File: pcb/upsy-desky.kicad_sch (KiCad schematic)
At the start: 44 parts, among them J1 RJ45, J2 RJ45, J3 USB_C_ReceptacleUSB2.0, Q1 MMBT3904, Q2 MMBT3904, Q3 2N7002, Q4 2N7002, Q5 2N7002, Q6 2N7002, Q7 2N7002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

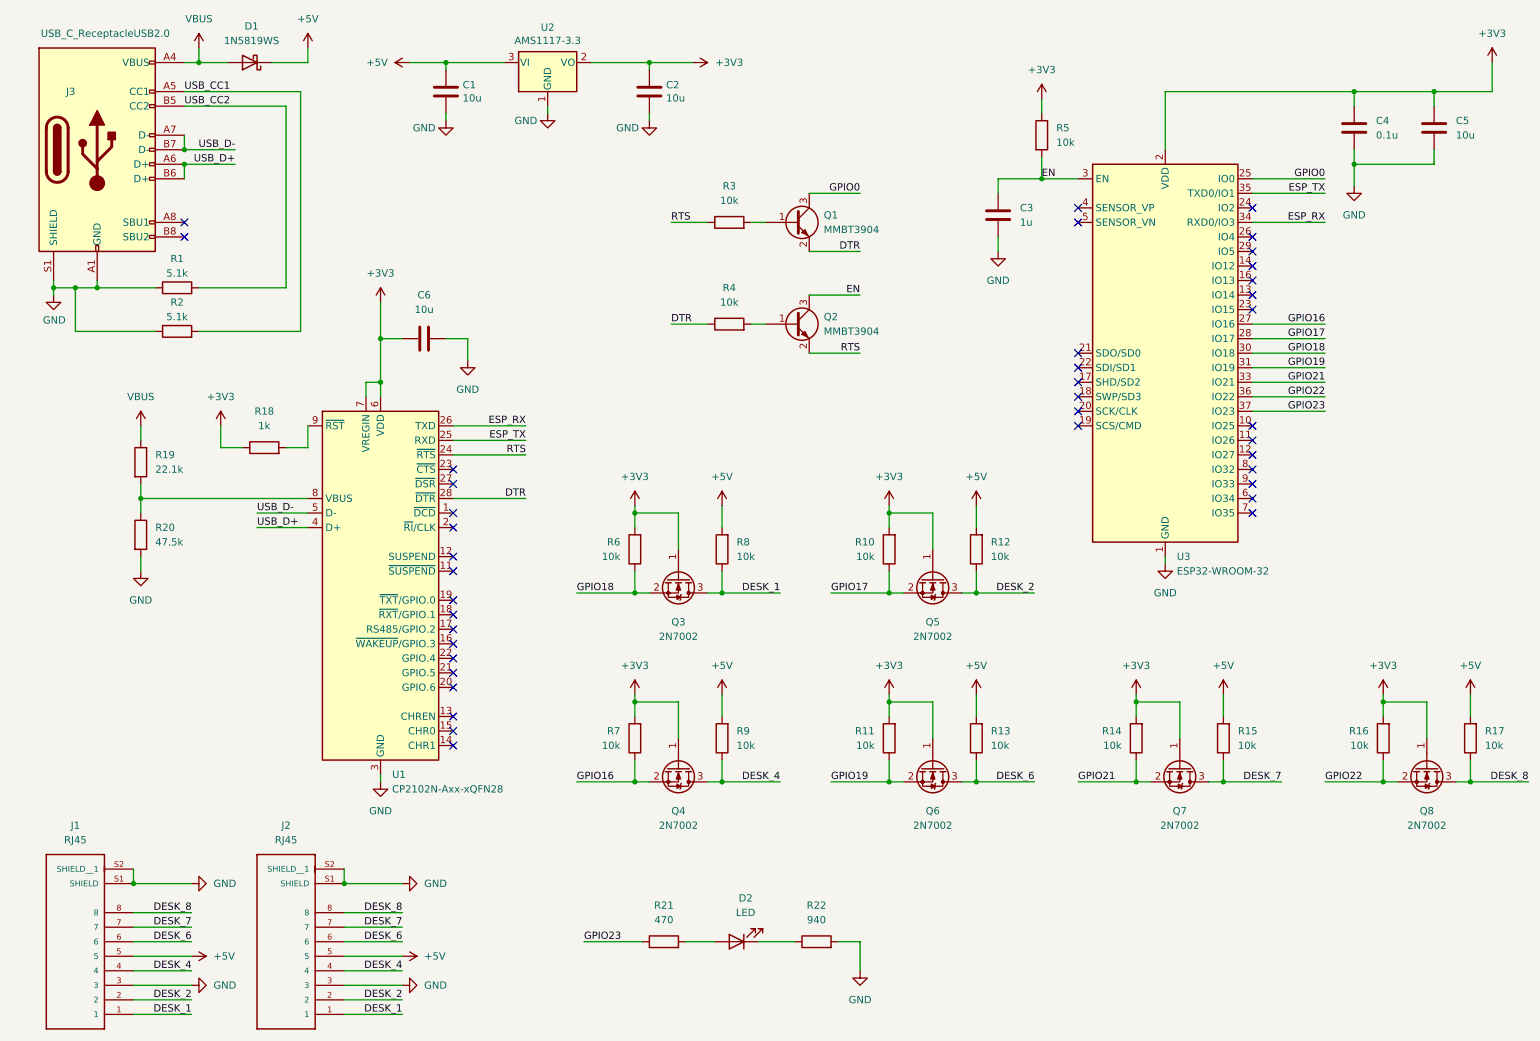
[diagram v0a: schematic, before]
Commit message: Adding updated PCB files using ESP32-s3-WROOM-1 MCU, removed UART to USB logic
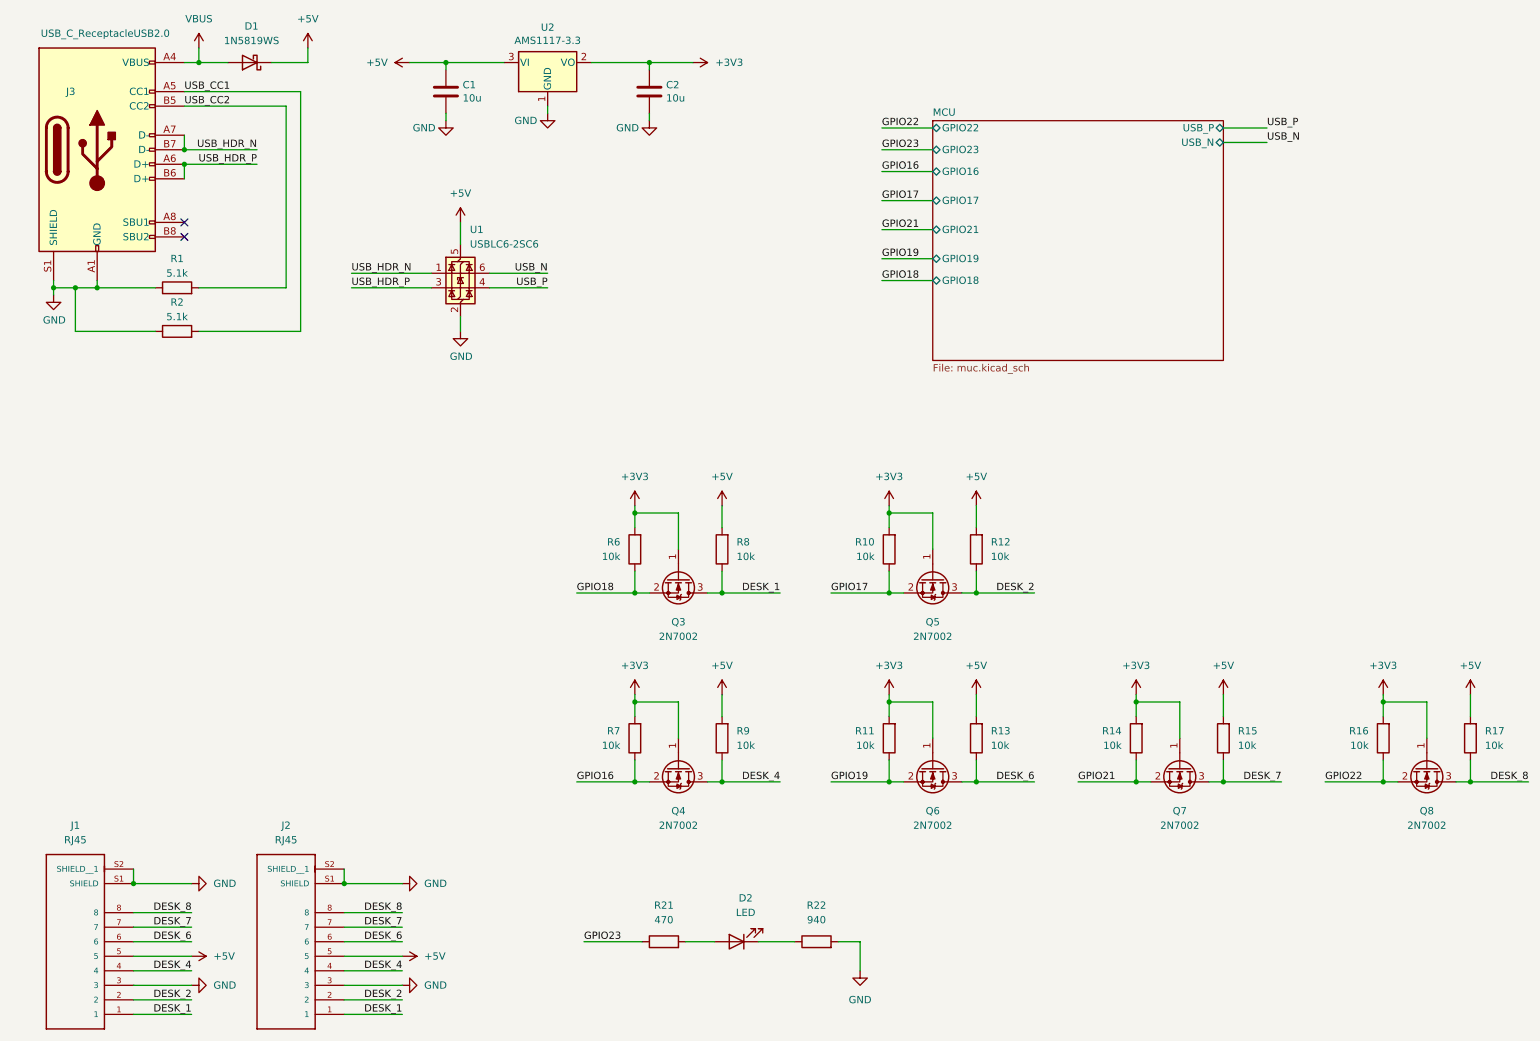
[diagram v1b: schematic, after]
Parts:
- removed C3: 1u, Capacitor_SMD:C_0402_1005Metric, symbol Device:C
- removed C4: 0.1u, Capacitor_SMD:C_0402_1005Metric, symbol Device:C
- removed C5, C6: 10u, Capacitor_SMD:C_0402_1005Metric, symbol Device:C
- removed Q1, Q2: MMBT3904, Package_TO_SOT_SMD:SOT-23, symbol Transistor_BJT:MMBT3904
- removed R18: 1k, Resistor_SMD:R_0402_1005Metric, symbol Device:R
- removed R19: 22.1k, Resistor_SMD:R_0402_1005Metric, symbol Device:R
- removed R20: 47.5k, Resistor_SMD:R_0402_1005Metric, symbol Device:R
- removed R3, R4, R5: 10k, Resistor_SMD:R_0402_1005Metric, symbol Device:R
- removed U1: CP2102N-Axx-xQFN28, Package_DFN_QFN:QFN-28-1EP_5x5mm_P0.5mm_EP3.35x3.35mm, symbol Interface_USB:CP2102N-Axx-xQFN28
- removed U3: ESP32-WROOM-32, RF_Module:ESP32-WROOM-32, symbol RF_Module:ESP32-WROOM-32
- added U1: USBLC6-2SC6, Package_TO_SOT_SMD:SOT-23-6, symbol Power_Protection:USBLC6-2SC6
- J1, J2: LCSC C3000202 -> C708595
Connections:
- net +5V: now also U1.5 (VBUS)
- net GND: now also U1.2 (GND)
- net USB_D+ renamed USB_HDR_P
- net USB_HDR_P: now also U1.3 (I/O2)
- net USB_D- renamed USB_HDR_N
- net USB_HDR_N: now also U1.1 (I/O1)
- new net USB_N: U1.6 (I/O1)
- new net USB_P: U1.4 (I/O2)
- no-connect marks 40 -> 2
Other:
- added sheet MCU (muc.kicad_sch)
